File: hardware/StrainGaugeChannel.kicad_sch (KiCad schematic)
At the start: 21 parts, among them J6 Conn_02x05_Odd_Even, U5 TS5A3166DBVR, U6 ADS1220xPW

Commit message: sath rev
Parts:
- R24, R25, R26, R27: value DNP -> (none); now not fitted
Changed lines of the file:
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@@
 		(on_board yes)
 		(in_pos_files yes)
-		(dnp no)
+		(dnp yes)
 		(fields_autoplaced yes)
 		(property "Reference" "R24"
-			(at 170.18 62.2299 0)
+			(at 170.18 63.4999 0)
 			(show_name no)
 			(do_not_autoplace no)
@@
 			)
 		)
-		(property "Value" "DNP"
+		(property "Value" ""
 			(at 170.18 64.7699 0)
 			(show_name no)
@@
 		(on_board yes)
 		(in_pos_files yes)
-		(dnp no)
+		(dnp yes)
 		(fields_autoplaced yes)
 		(property "Reference" "R27"
-			(at 190.5 78.7399 0)
+			(at 190.5 80.0099 0)
 			(show_name no)
 			(do_not_autoplace no)
@@
 			)
 		)
-		(property "Value" "DNP"
+		(property "Value" ""
 			(at 190.5 81.2799 0)
 			(show_name no)
@@
 		(on_board yes)
 		(in_pos_files yes)
-		(dnp no)
+		(dnp yes)
 		(fields_autoplaced yes)
 		(property "Reference" "R25"
-			(at 190.5 62.2299 0)
+			(at 190.5 63.4999 0)
 			(show_name no)
 			(do_not_autoplace no)
@@
 			)
 		)
-		(property "Value" "DNP"
+		(property "Value" ""
 			(at 190.5 64.7699 0)
 			(show_name no)
@@
 		(on_board yes)
 		(in_pos_files yes)
-		(dnp no)
+		(dnp yes)
 		(fields_autoplaced yes)
 		(property "Reference" "R26"
-			(at 170.18 78.7399 0)
+			(at 170.18 80.0099 0)
 			(show_name no)
 			(do_not_autoplace no)
@@
 			)
 		)
-		(property "Value" "DNP"
+		(property "Value" ""
 			(at 170.18 81.2799 0)
 			(show_name no)

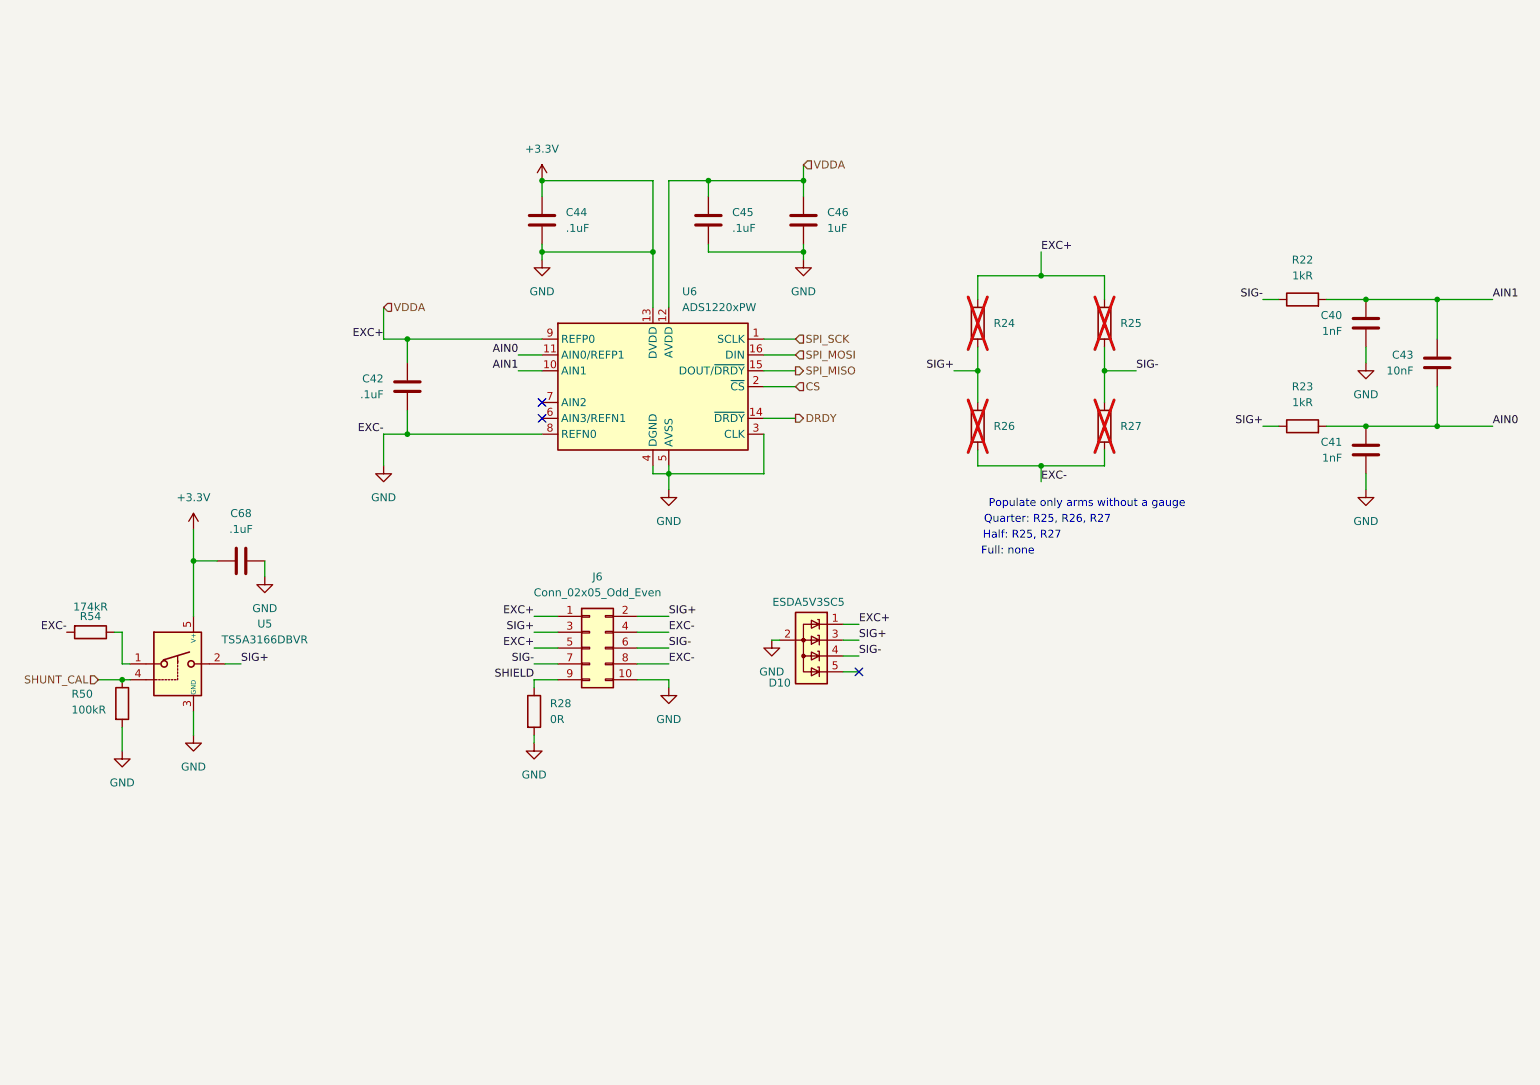
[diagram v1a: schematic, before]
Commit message: Update power mux and strain gauge channel schematics
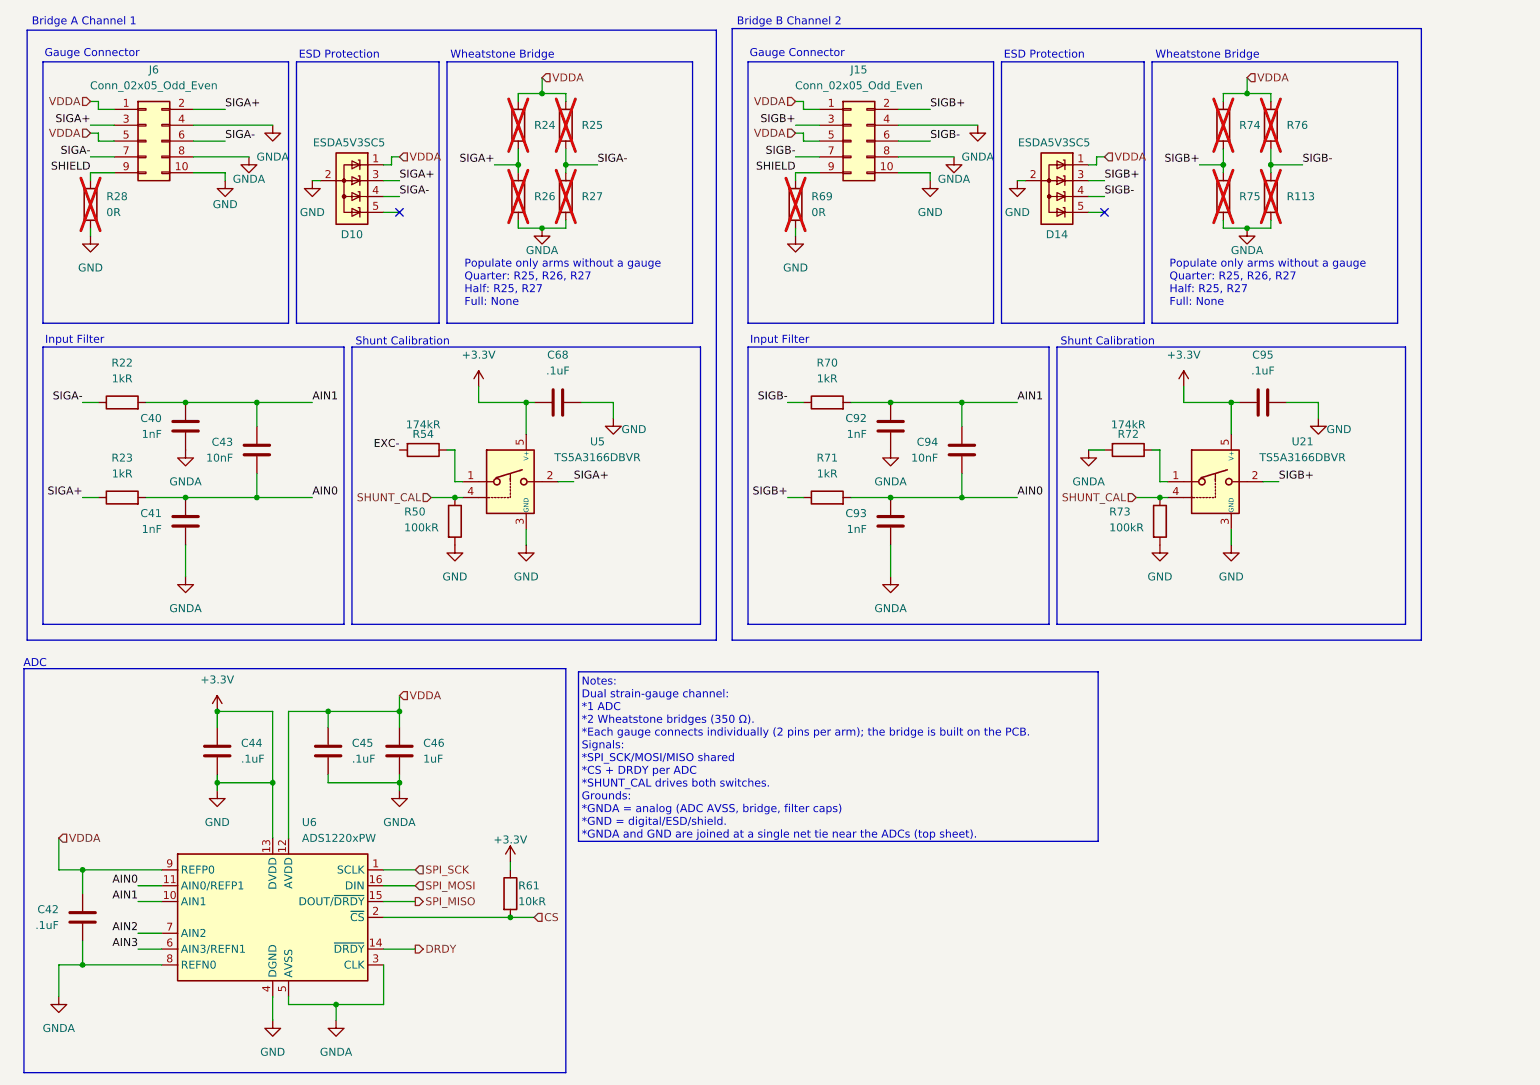
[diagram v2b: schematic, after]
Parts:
- added C92, C93: 1nF, symbol Device:C
- added C94: 10nF, symbol Device:C
- added C95: .1uF, symbol Device:C
- added D14: ESDA5V3SC5, Package_TO_SOT_SMD:SOT-23-5, symbol Power_Protection:ESDA5V3SC5
- added J15: Conn_02x05_Odd_Even, symbol Connector_Generic:Conn_02x05_Odd_Even
- added R113, R74, R75, R76: (no value), symbol Device:R
- added R61: 10kR, symbol Device:R
- added R69: 0R, symbol Device:R
- added R70, R71: 1kR, symbol Device:R
- added R72: 174kR, symbol Device:R
- added R73: 100kR, symbol Device:R
- added U21: TS5A3166DBVR, Package_TO_SOT_SMD:SOT-23-5, symbol Analog_Switch:TS5A3166DBVR
- R28: now not fitted
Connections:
- net +3.3V: now also C95.1, C95.2, D14.2 (A), J15.10 (Pin_10), R61.1, R69.2, R73.2, U21.3 (GND), U21.5 (V+); no longer C40.1, C41.1, C42.1, C45.2, C46.2, J6.4 (Pin_4), J6.8 (Pin_8), R26.2, R27.2, R54.2, U6.3 (CLK), U6.5 (AVSS), U6.8 (REFN0)
- net AIN0: now also C93.2, C94.1, R71.2
- net AIN1: now also C92.2, C94.2, R70.2
- net CS: now also R61.2
- net SHIELD: now also J15.9 (Pin_9), R69.1
- net SHUNT_CAL: now also R73.1, U21.4
- net VDDA: now also D14.1 (K), J15.1 (Pin_1), J15.5 (Pin_5), R74.1, R76.1
- net AIN3: now reaches U6.6 (AIN3/REFN1)
- net AIN2: now reaches U6.7 (AIN2)
- net SIG+ renamed SIGA+
- net SIG- renamed SIGA-
- new net: R72.1, U21.1
- new net EXC-: R54.2
- new net GNDA: C40.1, C41.1, C42.1, C45.2, C46.2, C92.1, C93.1, J15.4 (Pin_4), J15.8 (Pin_8), J6.4 (Pin_4), J6.8 (Pin_8), R113.2, R26.2, R27.2, R72.2, R75.2, U6.3 (CLK), U6.5 (AVSS), U6.8 (REFN0)
- new net SIGB+: D14.3 (K), J15.2 (Pin_2), J15.3 (Pin_3), R71.1, R74.2, R75.1, U21.2
- new net SIGB-: D14.4 (K), J15.6 (Pin_6), J15.7 (Pin_7), R113.1, R70.1, R76.2
- no-connect marks 3 -> 2
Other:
- note added: "ADC"
- note added: "Bridge A Channel 1"
- note added: "Bridge B Channel 2"
- note added: "ESD Protection"
- note added: "Gauge Connector"
- note added: "Input Filter"
- note added: "Notes: Dual strain-gauge channel: *1 ADC *2 Wheatstone bridges (350 Ω). *Each gauge connects individually (2 pins per arm); the bridge is built on the PCB. Signals: *SPI_SCK/MOSI/MISO shared *CS + DRDY per ADC *SHUNT_CAL drives both switches. Grounds: *GNDA = analog (ADC AVSS, bridge, filter caps) *GND = digital/ESD/shield. *GNDA and GND are joined at a single net tie near the ADCs (top sheet)."
- note added: "Populate only arms without a gauge Quarter: R25, R26, R27 Half: R25, R27 Full: None"
- note added: "Shunt Calibration"
- note added: "Wheatstone Bridge"
- note removed: "Full: none"
- note removed: "Half: R25, R27"
- note removed: "Populate only arms without a gauge"
- note removed: "Quarter: R25, R26, R27"
- moved on the sheet: C40, C41, C42, C43, C44, C45, C46, C68, D10, J6, R22, R23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

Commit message: Fixed ERC
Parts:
- added TP10, TP5, TP6, TP7, TP8, TP9: TestPoint, symbol Connector:TestPoint
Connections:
- net EXC- is gone; now on net GNDA: R54.2
- net +3.3V: no longer C44.2, C68.2, C95.2, D10.2 (A), D14.2 (A), J15.10 (Pin_10), J6.10 (Pin_10), R28.2, R50.2, R69.2, R73.2, U21.3 (GND), U5.3 (GND), U6.4 (DGND)
- net AIN0: no longer C93.2, C94.1, R71.2
- net AIN1: no longer C92.2, C94.2, R70.2
- net AIN2: now also C93.2, C94.1, R71.2
- net AIN3: now also C92.2, C94.2, R70.2
- net GNDA: now also TP6.1
- net SIGA+: now also TP7.1
- net SIGA-: now also TP8.1
- net SIGB+: now also TP9.1
- net SIGB-: now also TP10.1
- net VDDA: now also TP5.1
- net SHIELD renamed SHIELD A
- net SHIELD A: no longer J15.9 (Pin_9), R69.1
- new net GND: C44.2, C68.2, C95.2, D10.2 (A), D14.2 (A), J15.10 (Pin_10), J6.10 (Pin_10), R28.2, R50.2, R69.2, R73.2, U21.3 (GND), U5.3 (GND), U6.4 (DGND)
- new net SHIELD B: J15.9 (Pin_9), R69.1
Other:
- note added: "Test Points"
- note added: "check if you need an op amp"
- note added: "need more explaination"
- moved on the sheet: D10, D14, J15, J6, R113, R24, R25, R26, R27, R28, R50, R69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

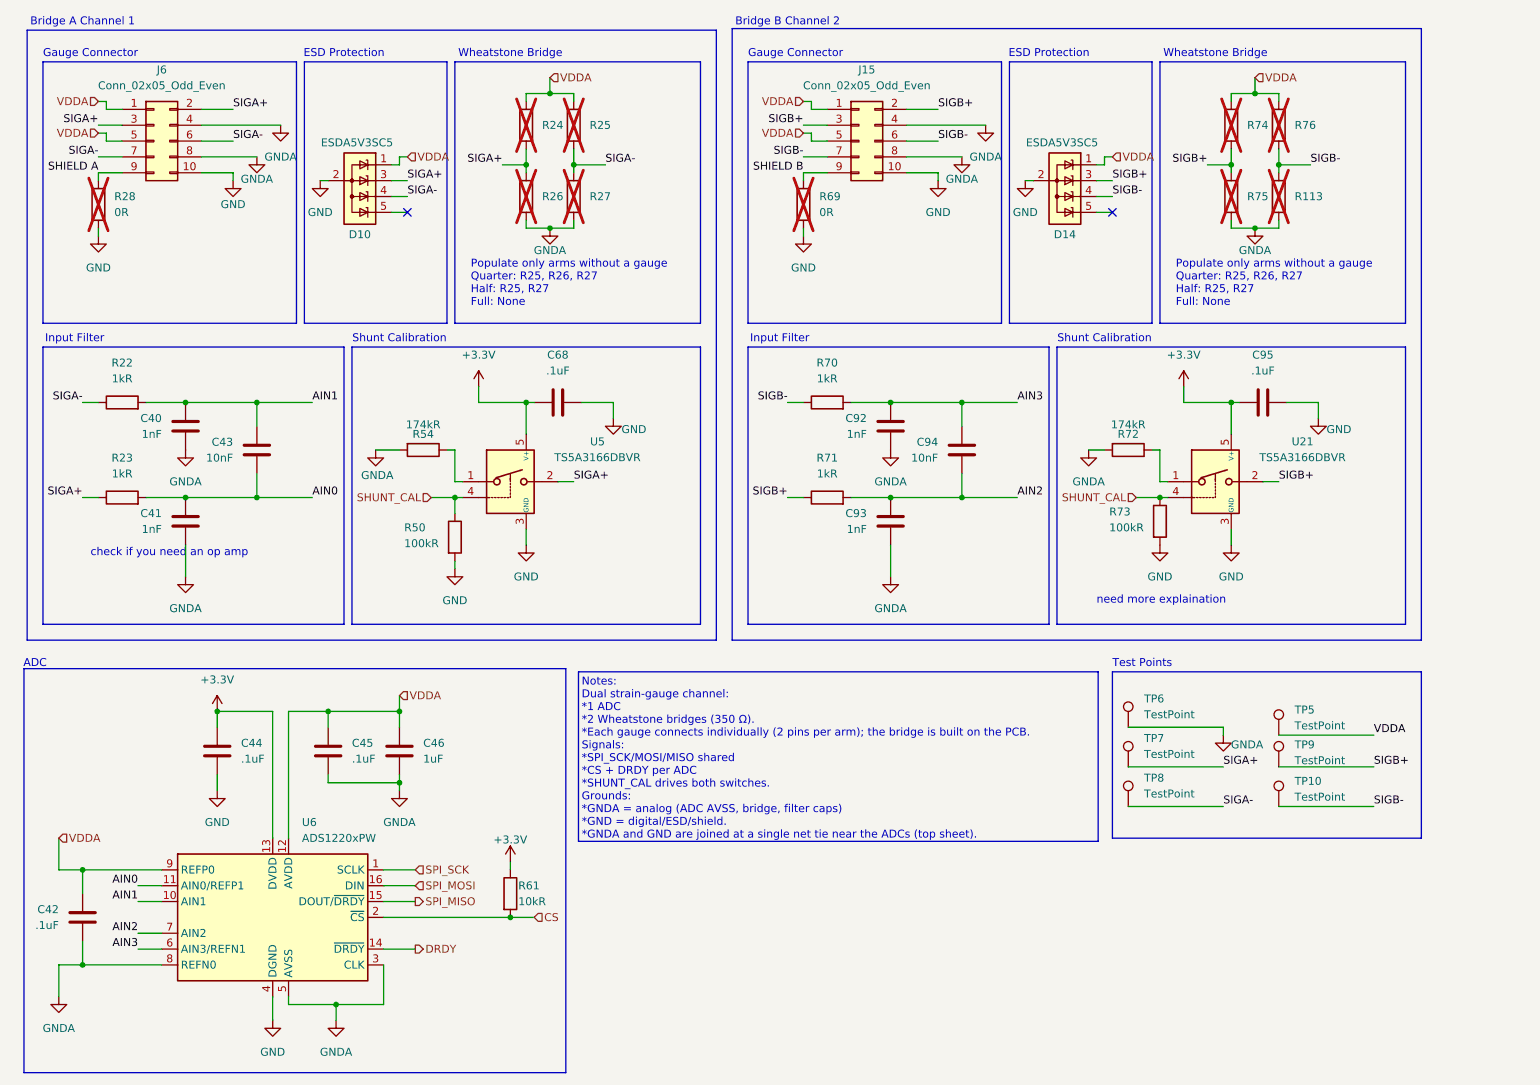
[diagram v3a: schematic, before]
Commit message: ELC review changes implemented
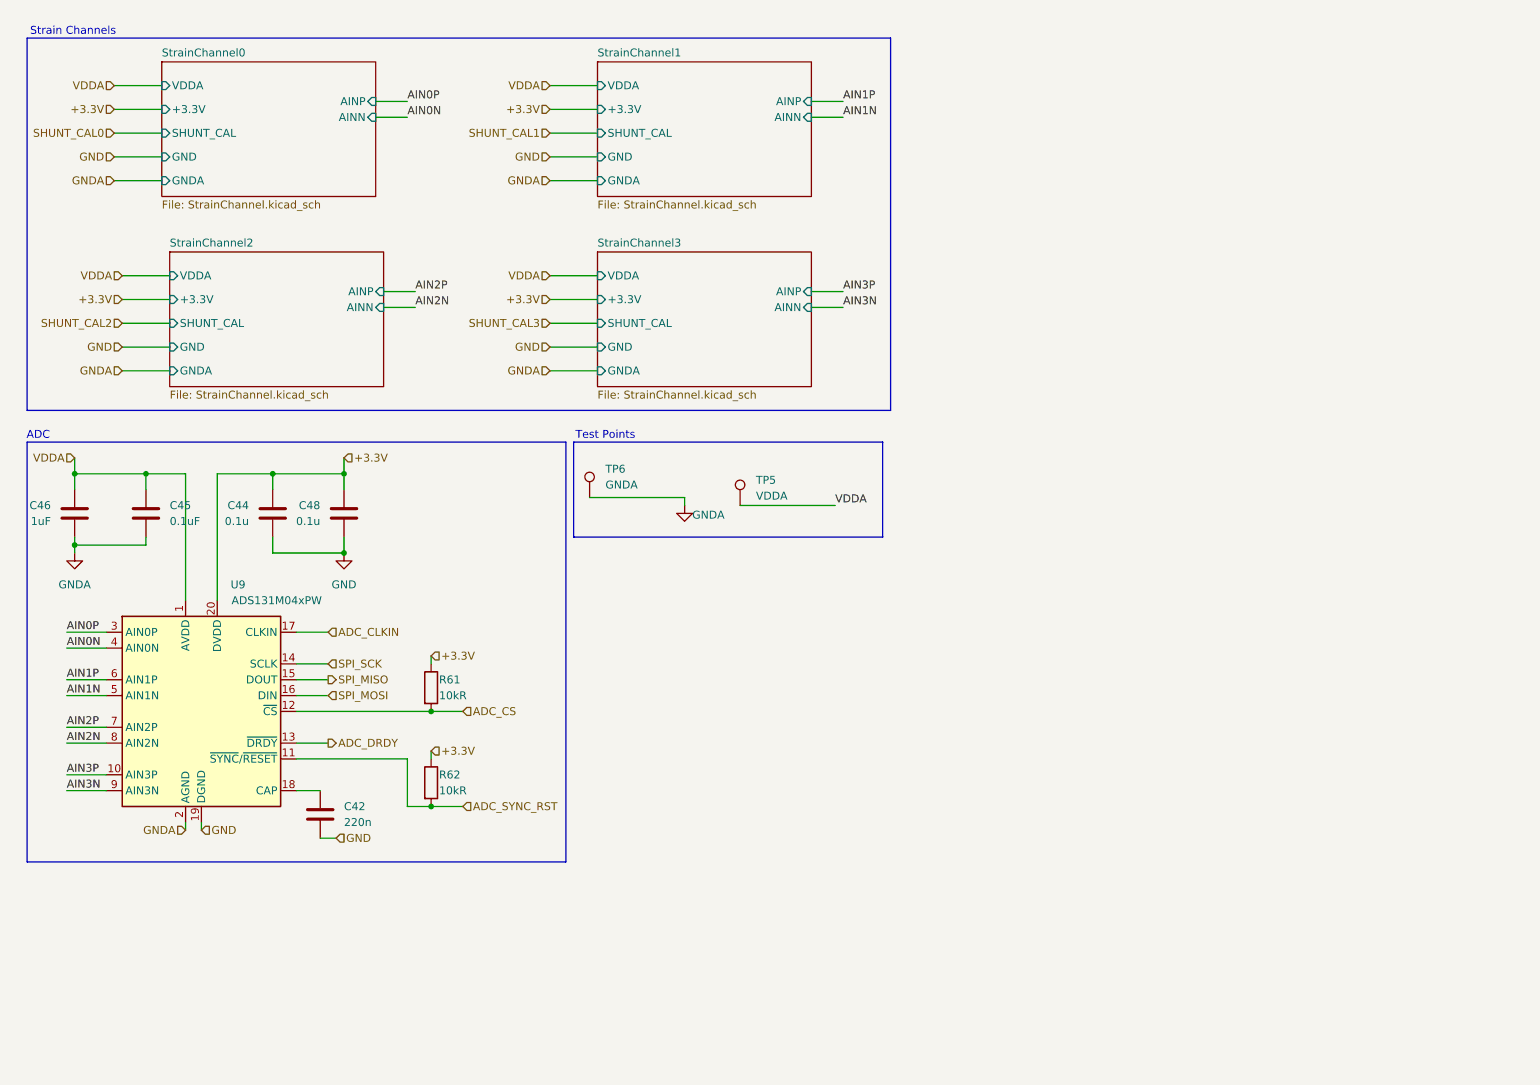
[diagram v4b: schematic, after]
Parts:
- removed C40, C41, C92, C93: 1nF, symbol Device:C
- removed C43, C94: 10nF, symbol Device:C
- removed C68, C95: .1uF, symbol Device:C
- removed D10, D14: ESDA5V3SC5, Package_TO_SOT_SMD:SOT-23-5, symbol Power_Protection:ESDA5V3SC5
- removed J15, J6: Conn_02x05_Odd_Even, symbol Connector_Generic:Conn_02x05_Odd_Even
- removed R113, R24, R25, R26, R27, R74, R75, R76: (no value), symbol Device:R
- removed R22, R23, R70, R71: 1kR, symbol Device:R
- removed R28, R69: 0R, symbol Device:R
- removed R50, R73: 100kR, symbol Device:R
- removed R54, R72: 174kR, symbol Device:R
- removed TP10, TP7, TP8, TP9: TestPoint, symbol Connector:TestPoint
- removed U21, U5: TS5A3166DBVR, Package_TO_SOT_SMD:SOT-23-5, symbol Analog_Switch:TS5A3166DBVR
- removed U6: ADS1220xPW, Package_SO:TSSOP-16_4.4x5mm_P0.65mm, symbol Analog_ADC:ADS1220xPW
- added C48: 0.1u, symbol Device:C
- added R62: 10kR, symbol Device:R
- added U9: ADS131M04xPW, Package_SO:TSSOP-20_4.4x6.5mm_P0.65mm, symbol Analog_ADC:ADS131M04xPW
- C42: value .1uF -> 220n
- C44: value .1uF -> 0.1u
- C45: value .1uF -> 0.1uF
- TP5: value TestPoint -> VDDA
- TP6: value TestPoint -> GNDA
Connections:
- net +3.3V: now also C48.1, R62.1, U9.20 (DVDD)
- net GND: now also C42.2, C48.2, U9.19 (DGND)
- net GNDA: now also U9.2 (AGND); no longer C42.1
- net SPI_MISO: now also U9.15 (DOUT)
- net SPI_MOSI: now also U9.16 (DIN)
- net SPI_SCK: now also U9.14 (SCLK)
- net VDDA: now also U9.1 (AVDD); no longer C42.2
- net CS renamed ADC_CS
- net ADC_CS: now also U9.12 (~{CS})
- new net: C42.1, U9.18 (CAP)
- new net ADC_CLKIN: U9.17 (CLKIN)
- new net ADC_DRDY: U9.13 (~{DRDY})
- new net ADC_SYNC_RST: R62.2, U9.11 (~{SYNC}/~{RESET})
- new net AIN0N: U9.4 (AIN0N)
- new net AIN0P: U9.3 (AIN0P)
- new net AIN1N: U9.5 (AIN1N)
- new net AIN1P: U9.6 (AIN1P)
- new net AIN2N: U9.8 (AIN2N)
- new net AIN2P: U9.7 (AIN2P)
- new net AIN3N: U9.9 (AIN3N)
- new net AIN3P: U9.10 (AIN3P)
- no-connect marks 2 -> 0
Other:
- added sheet StrainChannel0 (StrainChannel.kicad_sch)
- added sheet StrainChannel1 (StrainChannel.kicad_sch)
- added sheet StrainChannel2 (StrainChannel.kicad_sch)
- added sheet StrainChannel3 (StrainChannel.kicad_sch)
- note added: "Strain Channels"
- note removed: "Bridge A Channel 1"
- note removed: "Bridge B Channel 2"
- note removed: "ESD Protection"
- note removed: "Gauge Connector"
- note removed: "Input Filter"
- note removed: "Notes: Dual strain-gauge channel: *1 ADC *2 Wheatstone bridges (350 Ω). *Each gauge connects individually (2 pins per arm); the bridge is built on the PCB. Signals: *SPI_SCK/MOSI/MISO shared *CS + DRDY per ADC *SHUNT_CAL drives both switches. Grounds: *GNDA = analog (ADC AVSS, bridge, filter caps) *GND = digital/ESD/shield. *GNDA and GND are joined at a single net tie near the ADCs (top sheet)."
- note removed: "Populate only arms without a gauge Quarter: R25, R26, R27 Half: R25, R27 Full: None"
- note removed: "Shunt Calibration"
- note removed: "Wheatstone Bridge"
- note removed: "check if you need an op amp"
- note removed: "need more explaination"
- moved on the sheet: TP5, TP6
